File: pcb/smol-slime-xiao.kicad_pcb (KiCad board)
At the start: 4 copper layers, 17.5 x 21 mm, 6 parts, among them U1 ICM-45686

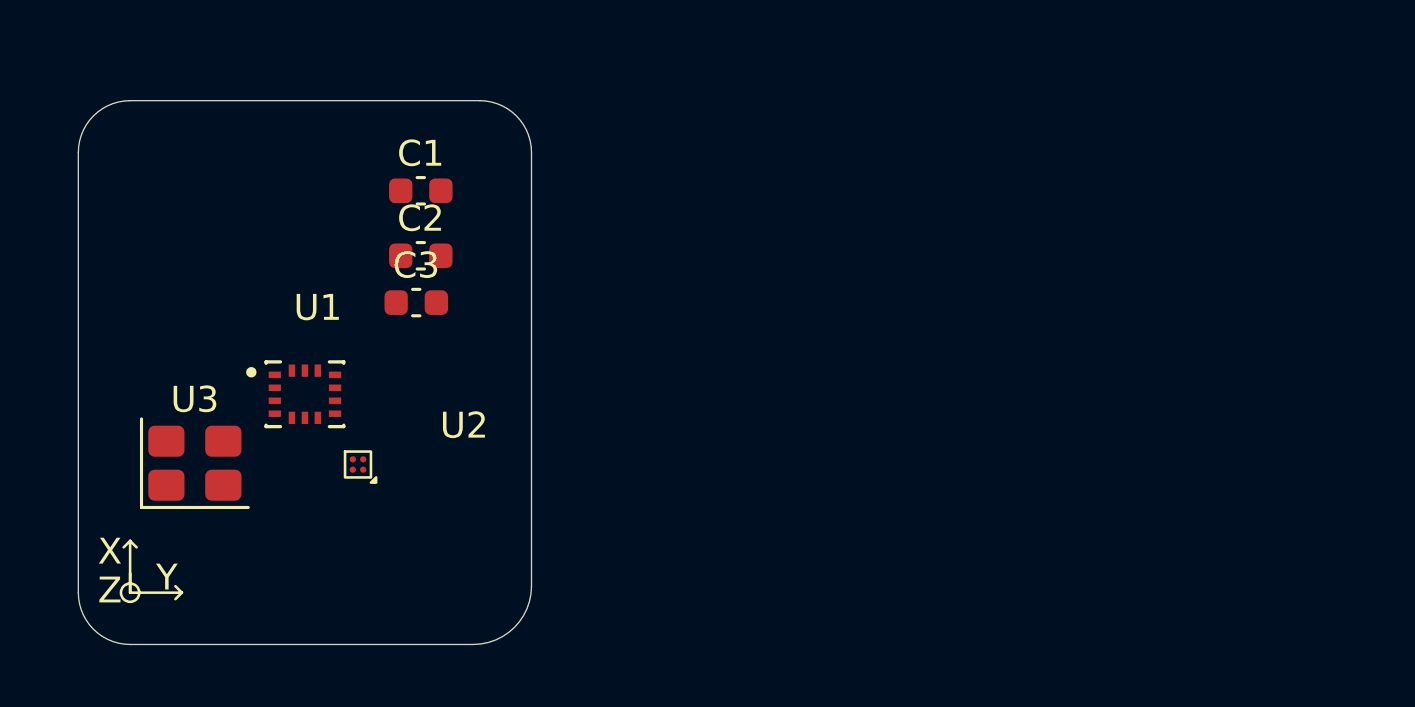
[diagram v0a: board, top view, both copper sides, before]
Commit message: Add XIAO MCU symbol
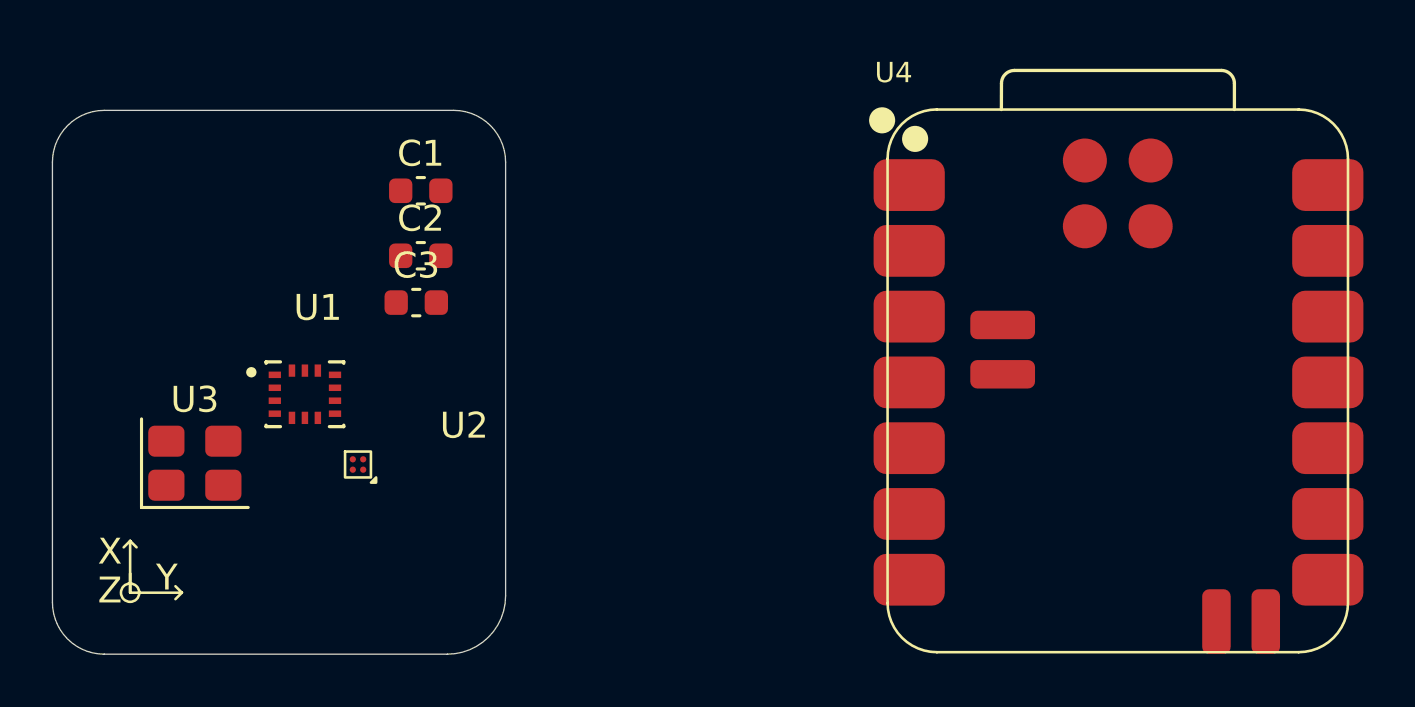
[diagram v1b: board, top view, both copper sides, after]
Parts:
- added U4: XIAO-nRF52840-SMD, Seeed Studio XIAO Series Library:XIAO-nRF52840-SMD, F.Cu at (178.7, 103.9)
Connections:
- C3 pad 1: Net-(U2-VDD) -> VDD
- C3 pad 2: Net-(U2-VSS) -> GND
- U2 pad A1: Net-(U2-VSS) -> GND
- U2 pad B1: Net-(U2-VDD) -> VDD

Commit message: Update components
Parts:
- added R1: 10K, Resistor_SMD:R_0603_1608Metric, F.Cu at (158.9, 117.0)
- added R2: 10K, Resistor_SMD:R_0603_1608Metric, F.Cu at (158.9, 119.5)
- added R3: 10K, Resistor_SMD:R_0603_1608Metric, F.Cu at (158.9, 122.0)
- U3: value ~ -> 1532H
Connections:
- C3 pad 1: VDD -> GND
- C3 pad 2: GND -> VDD
- U1 pad 1: unconnected-(U1-AP_SDO/AP_AD0-Pad1) -> /SPI_MISO
- U1 pad 12: unconnected-(U1-AP_CS-Pad12) -> /SPI_CS_IMU
- U1 pad 13: unconnected-(U1-AP_SCL/AP_SCLK-Pad13) -> /SPI_SCK
- U1 pad 14: unconnected-(U1-AP_SDA/AP_SDIO/AP_SDI-Pad14) -> /SPI_MOSI
- U1 pad 4: unconnected-(U1-INT1/INT-Pad4) -> /IMU_INT
- U1 pad 9: unconnected-(U1-INT2/FSYNC/CLKIN-Pad9) -> /IMU_CLKIN
- U2 pad A2: unconnected-(U2-SCL-PadA2) -> /I2C_SCL
- U2 pad B2: unconnected-(U2-SDA-PadB2) -> /I2C_SDA
- U3 pad 1: unconnected-(U3-ED-Pad1) -> /CLK_CTL
- U3 pad 2: unconnected-(U3-GND-Pad2) -> VDD
- U3 pad 3: unconnected-(U3-Output-Pad3) -> /IMU_CLKIN
- U3 pad 4: unconnected-(U3-VDD-Pad4) -> VDD
- U4 pad 10: unconnected-(U4-P1.14_D9_MISO-Pad10) -> /SPI_MISO
- U4 pad 11: unconnected-(U4-P1.15_D10_MOSI-Pad11) -> /SPI_MOSI
- U4 pad 12: unconnected-(U4-3V3-Pad12) -> VDD
- U4 pad 13: unconnected-(U4-GND-Pad13) -> GND
- U4 pad 14: unconnected-(U4-5V-Pad14) -> +5V
- U4 pad 15: unconnected-(U4-BAT-Pad15) -> Net-(J1-Pin_2)
- U4 pad 16: unconnected-(U4-GND-Pad16) -> GND
- U4 pad 22: unconnected-(U4-GND-Pad22) -> GND
- U4 pad 3: unconnected-(U4-P0.28_A2_D2-Pad3) -> /SPI_CS_IMU
- U4 pad 4: unconnected-(U4-P0.29_A3_D3-Pad4) -> /IMU_INT
- U4 pad 5: unconnected-(U4-P0.04_A4_D4_SDA-Pad5) -> /I2C_SDA
- U4 pad 6: unconnected-(U4-P0.05_A5_D5_SCL-Pad6) -> /I2C_SCL
- U4 pad 7: unconnected-(U4-P1.11_D6_TX-Pad7) -> /CLK_CTL
- U4 pad 9: unconnected-(U4-P1.13_D8_SCK-Pad9) -> /SPI_SCK

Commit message: Roughly lay out components
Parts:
- U4: moved to B.Cu
- moved U3 53.2 mm to (196.2, 106.4), turned to 180 degrees
- moved C3 42.4 mm to (191.0, 116.2), turned to 90 degrees
- moved U1 42.3 mm to (189.5, 106.5)
- moved R3 42.0 mm to (196.2, 102.8)
- moved C1 41.5 mm to (191.0, 110.0), turned to 90 degrees
- moved U2 40.7 mm to (188.9, 116.3)
- moved C2 38.9 mm to (189.0, 110.0), turned to 90 degrees
- moved R1 27.4 mm to (186.2, 114.5)
- moved R2 27.4 mm to (186.2, 117.2)
- moved U4 11.1 mm to (189.5, 106.5), turned to 180 degrees
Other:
- board size 17.5 x 21 mm -> 97.5 x 35.8 mm

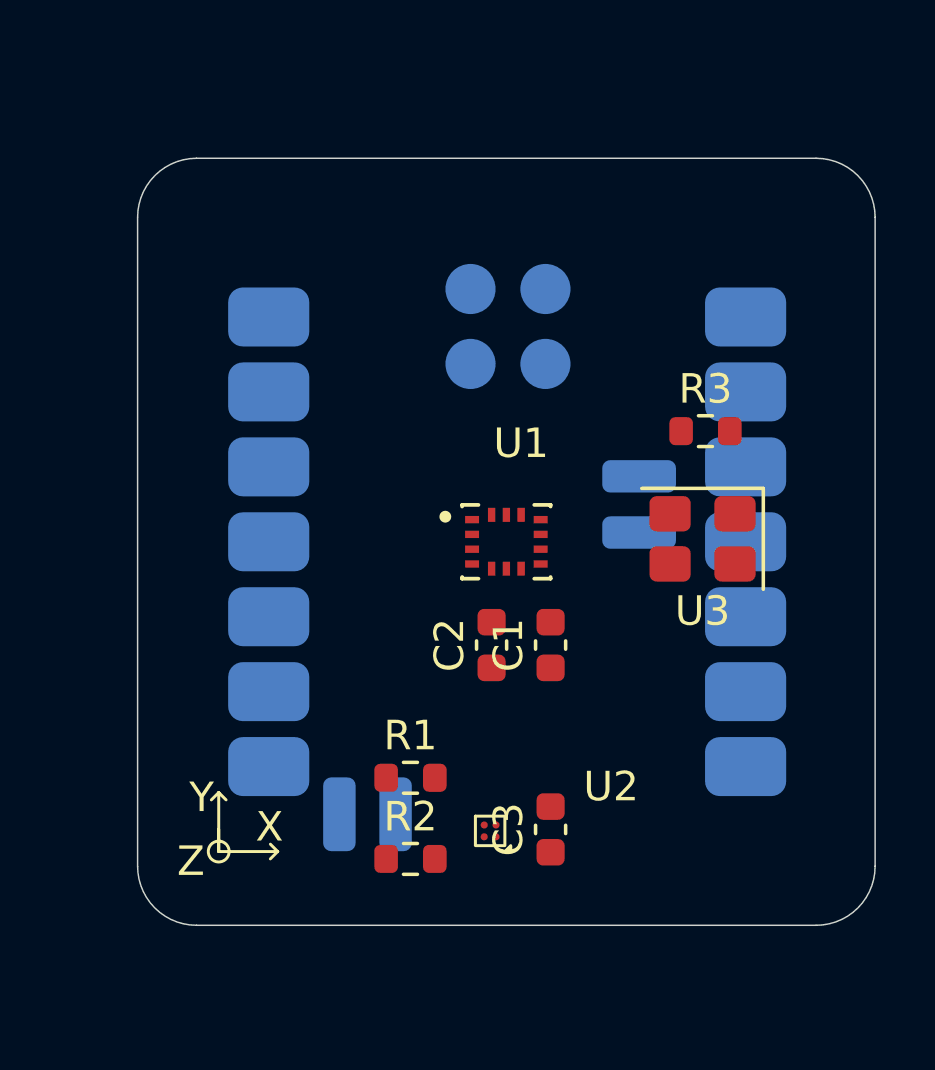
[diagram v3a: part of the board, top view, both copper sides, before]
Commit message: Re-arrange for optimal magnetometer placement
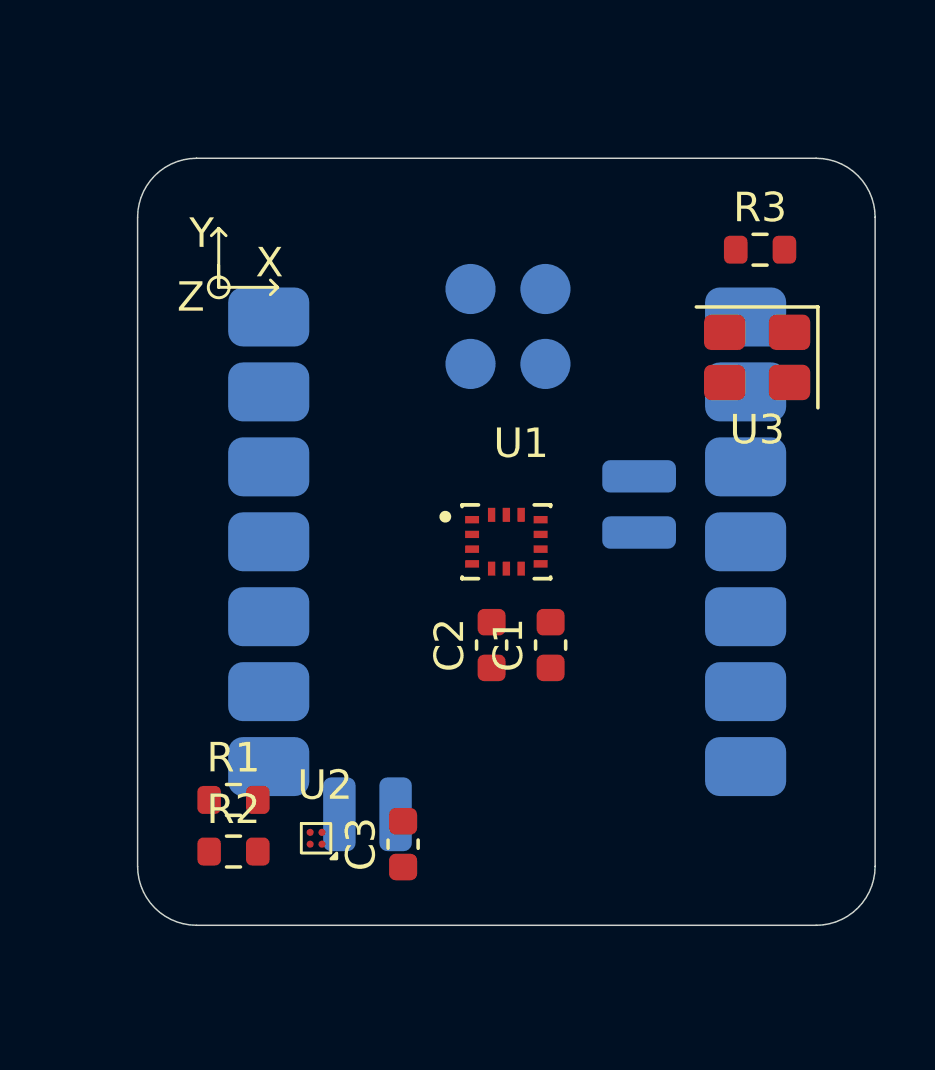
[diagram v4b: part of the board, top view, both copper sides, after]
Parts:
- moved R3 6.42 mm to (198.1, 96.6)
- moved U3 6.42 mm to (198.0, 100.2)
- moved R1 6.05 mm to (180.2, 115.2)
- moved R2 6.01 mm to (180.2, 117.0)
- moved U2 5.91 mm to (183.1, 116.5)
- moved C3 5.02 mm to (186.0, 116.8)
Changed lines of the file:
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@@
 	(footprint "Resistor_SMD:R_0603_1608Metric"
 		(layer "F.Cu")
-		(at 196.25 102.75)
+		(at 198.1 96.6)
 		(descr "Resistor SMD 0603 (1608 Metric), square (rectangular) end terminal, IPC-7351 nominal, (Body size source: IPC-SM-782 page 72, https://www.pcb-3d.com/wordpress/wp-content/uploads/ipc-sm-782a_amendment_1_and_2.pdf), generated with kicad-footprint-generator")
 		(tags "resistor")
@@
 	(footprint "Resistor_SMD:R_0603_1608Metric"
 		(layer "F.Cu")
-		(at 186.25 117.25)
+		(at 180.25 117)
 		(descr "Resistor SMD 0603 (1608 Metric), square (rectangular) end terminal, IPC-7351 nominal, (Body size source: IPC-SM-782 page 72, https://www.pcb-3d.com/wordpress/wp-content/uploads/ipc-sm-782a_amendment_1_and_2.pdf), generated with kicad-footprint-generator")
 		(tags "resistor")
@@
 	(footprint "QMC6309:QMC6309"
 		(layer "F.Cu")
-		(at 188.95 116.3)
+		(at 183.05 116.55)
 		(property "Reference" "U2"
-			(at 4.1 -1.5 0)
+			(at 0.3 -1.8 0)
 			(unlocked yes)
 			(layer "F.SilkS")
@@
 		)
 		(property "Value" "~"
-			(at 4.1 0 0)
+			(at 2.05 -1.55 0)
 			(unlocked yes)
 			(layer "F.Fab")
@@
 		)
 		(fp_text user "${REFERENCE}"
-			(at 4.1 1.5 0)
+			(at 3.3 -1.8 0)
 			(unlocked yes)
 			(layer "F.Fab")
@@
 	(footprint "Crystal:Crystal_SMD_3225-4Pin_3.2x2.5mm"
 		(layer "F.Cu")
-		(at 196.15 106.4 180)
+		(at 198 100.25 180)
 		(descr "SMD3225/4, Crystal, 3.2x2.5mm package, SMD, generated with kicad-footprint-generator make_crystal.py, http://www.txccrystal.com/images/pdf/7m-accuracy.pdf")
 		(property "Reference" "U3"
@@
 	(footprint "Capacitor_SMD:C_0603_1608Metric"
 		(layer "F.Cu")
-		(at 191 116.25 90)
+		(at 186 116.75 90)
 		(descr "Capacitor SMD 0603 (1608 Metric), square (rectangular) end terminal, IPC-7351 nominal, (Body size source: IPC-SM-782 page 76, https://www.pcb-3d.com/wordpress/wp-content/uploads/ipc-sm-782a_amendment_1_and_2.pdf), generated with kicad-footprint-generator")
 		(tags "capacitor")
@@
 	(footprint "Resistor_SMD:R_0603_1608Metric"
 		(layer "F.Cu")
-		(at 186.25 114.5)
+		(at 180.25 115.25)
 		(descr "Resistor SMD 0603 (1608 Metric), square (rectangular) end terminal, IPC-7351 nominal, (Body size source: IPC-SM-782 page 72, https://www.pcb-3d.com/wordpress/wp-content/uploads/ipc-sm-782a_amendment_1_and_2.pdf), generated with kicad-footprint-generator")
 		(tags "resistor")
@@
 	)
 	(gr_line
-		(start 179.75 116.25)
-		(end 179.75 117)
+		(start 179.75 97.125)
+		(end 179.75 97.875)
 		(stroke
 			(width 0.1)
@@
 	)
 	(gr_line
-		(start 181.75 117)
-		(end 179.75 117)
+		(start 181.75 97.875)
+		(end 179.75 97.875)
 		(stroke
 			(width 0.1)
@@
 	)
 	(gr_line
-		(start 181.75 117)
-		(end 181.5 116.75)
+		(start 181.75 97.875)
+		(end 181.5 97.625)
 		(stroke
 			(width 0.1)
@@
 	)
 	(gr_circle
-		(center 179.75 117)
-		(end 180 116.75)
+		(center 179.75 97.875)
+		(end 180 97.625)
 		(stroke
 			(width 0.1)
@@
 	)
 	(gr_line
-		(start 179.75 117)
-		(end 179.75 115)
+		(start 179.75 97.875)
+		(end 179.75 95.875)
 		(stroke
 			(width 0.1)
@@
 	)
 	(gr_line
-		(start 181.75 117)
-		(end 181.5 117.25)
+		(start 181.75 97.875)
+		(end 181.5 98.125)
 		(stroke
 			(width 0.1)
@@
 	)
 	(gr_line
-		(start 179.75 115)
-		(end 179.5 115.25)
+		(start 179.75 95.875)
+		(end 179.5 96.125)
 		(stroke
 			(width 0.1)
@@
 	)
 	(gr_line
-		(start 179.75 115)
-		(end 180 115.25)
+		(start 179.75 95.875)
+		(end 180 96.125)
 		(stroke
 			(width 0.1)
@@
 	)
 	(gr_text "X"
-		(at 181 116.75 0)
+		(at 181 97.625 0)
 		(layer "F.SilkS")
 		(effects
@@
 	)
 	(gr_text "Z"
-		(at 178.335787 117.914214 0)
+		(at 178.335787 98.789214 0)
 		(layer "F.SilkS")
 		(effects
@@
 	)
 	(gr_text "Y"
-		(at 178.75 115.75 0)
+		(at 178.75 96.625 0)
 		(layer "F.SilkS")
 		(effects
@@
 		)
 	)
+	(group ""
+		(members "0fada15b-2bc5-4fbc-bba3-ab1a9c49d1df" "1d7cc48a-e6c3-4bbc-b7b1-96e232fcad8a"
+			"261c733e-e8fe-40a2-87e2-0d8430dc5ef1" "2815047a-9d89-4903-8800-25c410908a4b"
+			"45d415e5-5326-412a-bc72-edf0c8e0c47a" "5791a907-d210-4d49-85fe-749d39e47706"
+			"5be56eaf-233f-4d99-a3c7-283121f79f85" "7194b3cb-35a6-4cab-96c0-39e635ba88ee"
+			"81aaaac9-cd3f-4afb-a484-654d38838b0c" "94c5a510-21b7-4f26-a7a6-68aeed837478"
+			"c656faed-d832-4548-93da-f09dd41c0729"
+		)
+	)

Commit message: Fix edge cuts
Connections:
- net Net-(J1-Pin_2) renamed /VBAT
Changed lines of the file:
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@@
 	(net 17 "/SPI_MOSI")
 	(net 18 "+5V")
-	(net 19 "Net-(J1-Pin_2)")
+	(net 19 "/VBAT")
 	(net 20 "unconnected-(C2-Pad1)")
 	(net 21 "unconnected-(U4-P1.12_D7_RX-Pad8)")
@@
 			(layers "B.Cu" "B.Mask" "B.Paste")
 			(roundrect_rratio 0.25)
-			(net 19 "Net-(J1-Pin_2)")
+			(net 19 "/VBAT")
 			(pinfunction "BAT")
 			(pintype "passive")
